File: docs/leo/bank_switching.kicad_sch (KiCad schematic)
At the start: 5 parts, among them IC28 74LS138, IC35 74LS175, IC36 74LS157, J16 Jumper_3_Open, J20 Jumper_3_Bridged12

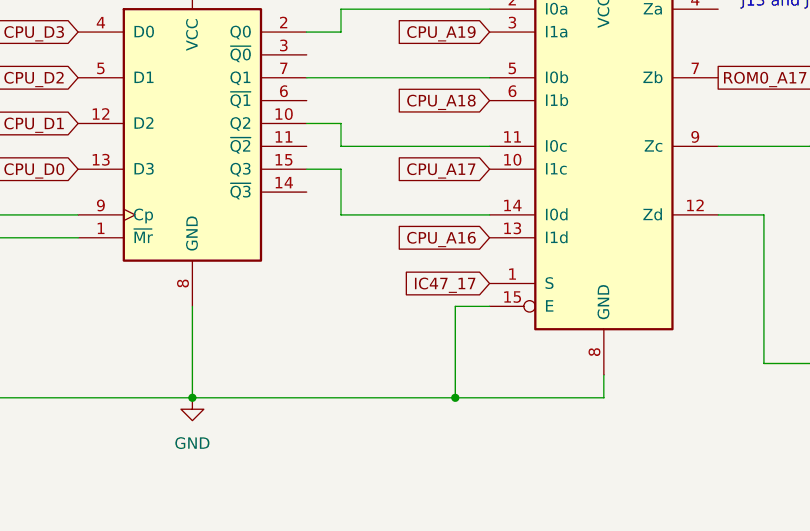
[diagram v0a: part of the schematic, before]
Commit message: Decode M92-B-7H-D PAL
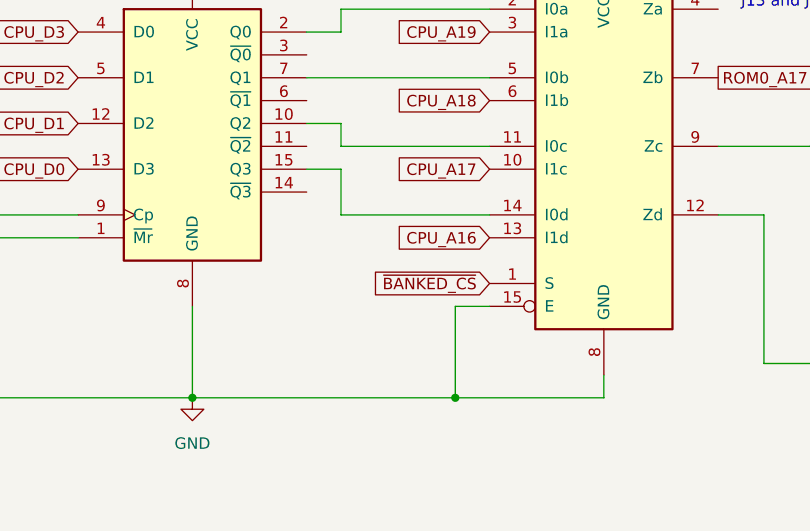
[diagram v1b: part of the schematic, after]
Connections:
- net IC47_17 renamed ~{BANKED_CS}
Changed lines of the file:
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@@
     )
   )
-  (global_label "IC47_17" (shape input) (at 181.61 114.3 180) (fields_autoplaced)
+  (global_label "~{BANKED_CS}" (shape input) (at 181.61 114.3 180) (fields_autoplaced)
     (effects (font (size 1.27 1.27)) (justify right))
-    (property "Intersheet References" "${INTERSHEET_REFS}" (id 0) (at 171.5164 114.2206 0)
+    (property "Intersheet References" "${INTERSHEET_REFS}" (id 0) (at 168.3717 114.2206 0)
       (effects (font (size 1.27 1.27)) (justify right) hide)
     )
